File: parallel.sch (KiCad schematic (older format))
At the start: 76 parts, among them CN300 KEYBOARD, CN301 CENTRONICS, CN302 EXTERNAL FLOPPY, CN303 Conn_02x17_Odd_Even, J300 Conn_01x03_Male, J301 DF1:, Q301 2N3904, U102 GARY5719, U108 74LS74A, U203 74LS38, U300 CIA8520, U302 74LS32, U303 74F08, U607 74LS08, U900 74F00

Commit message: Misread the PCB; It's effectively E and not A1
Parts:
- removed C2: 270pF, symbol Device:C
- removed R3: 68, symbol Device:R
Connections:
- wire segments 614 -> 613
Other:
- note removed: "REV 6.2 fixes\n"the via" is A11 line tied to GND\nthrough C and R"
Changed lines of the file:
@@
 Text GLabel 15150 8250 2    50   Input ~ 0
 _BRST
-Entry Wire Line
-	1450 4350 1550 4450
-Wire Wire Line
-	1450 4350 1450 3600
-$Comp
-L Device:C C2
-U 1 1 5D447991
-P 1450 3450
-F 0 "C2" H 1565 3496 50  0000 L CNN
-F 1 "270pF" H 1565 3405 50  0000 L CNN
-F 2 "" H 1488 3300 50  0001 C CNN
-F 3 "~" H 1450 3450 50  0001 C CNN
-	1    1450 3450
-	1    0    0    -1
-$EndComp
-$Comp
-L Device:R R3
-U 1 1 5D4491FD
-P 1450 3150
-F 0 "R3" H 1520 3196 50  0000 L CNN
-F 1 "68" H 1520 3105 50  0000 L CNN
-F 2 "" V 1380 3150 50  0001 C CNN
-F 3 "~" H 1450 3150 50  0001 C CNN
-	1    1450 3150
-	1    0    0    -1
-$EndComp
-$Comp
-L power:GND #PWR0217
-U 1 1 5D44A7A4
-P 1450 3000
-F 0 "#PWR0217" H 1450 2750 50  0001 C CNN
-F 1 "GND" H 1455 2827 50  0000 C CNN
-F 2 "" H 1450 3000 50  0001 C CNN
-F 3 "" H 1450 3000 50  0001 C CNN
-	1    1450 3000
-	-1   0    0    1
-$EndComp
-Text Notes 1000 2700 0    50   ~ 0
-REV 6.2 fixes\n"the via" is A11 line tied to GND\nthrough C and R
 Text Notes 3050 6600 0    50   ~ 0
 REV 6.2 fixes list C909 as removed but I haven't seen\nit removed at all on numerous 6.2 boards.\nso it is kept here
@@
 Wire Bus Line
 	4950 5000 4950 5900
-Text Label 1450 3850 1    50   ~ 0
-A11
 $EndSCHEMATC

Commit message: Add gender to connectors
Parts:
- CN300, CN302: Gender (none) -> Female
- CN301: symbol Connector:DB25_Female -> Connector:DB25_Female_MountingHoles; Gender (none) -> Female
- CN303: Gender (none) -> Male
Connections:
- wire segments 613 -> 614
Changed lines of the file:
@@
 F 2 "" H 13100 2350 50  0001 C CNN
 F 3 " ~" H 13100 2350 50  0001 C CNN
+F 4 "Female" V 13150 2450 50  0001 C CNN "Gender"
 	1    13150 2450
 	0    -1   1    0
@@
 F 2 "" H 15650 5400 50  0001 C CNN
 F 3 "~" H 15650 5400 50  0001 C CNN
+F 4 "Male" H 15650 5400 50  0001 C CNN "Gender"
 	1    15650 5400
 	-1   0    0    -1
 $EndComp
 $Comp
-L Connector:DB25_Female CN301
+L Connector:DB25_Female_MountingHoles CN301
 U 1 1 6B84D7F5
 P 9150 5750
@@
 F 2 "" H 9150 5750 50  0001 C CNN
 F 3 " ~" H 9150 5750 50  0001 C CNN
+F 4 "Female" H 9150 5750 50  0001 C CNN "Gender"
 	1    9150 5750
 	1    0    0    -1
@@
 F 2 "" H 10100 1200 50  0001 C CNN
 F 3 "http://www.mouser.com/ds/2/18/40_c091_abd_e-75918.pdf" H 10100 1200 50  0001 C CNN
+F 4 "Female" H 10100 1200 50  0001 C CNN "Gender"
 	1    10100 1200
 	1    0    0    1
@@
 L power:GND #PWR0182
 U 1 1 6B8C755F
-P 8750 7150
-F 0 "#PWR0182" H 8750 6900 50  0001 C CNN
-F 1 "GND" H 8755 6977 50  0000 C CNN
-F 2 "" H 8750 7150 50  0001 C CNN
-F 3 "" H 8750 7150 50  0001 C CNN
-	1    8750 7150
+P 8750 7200
+F 0 "#PWR0182" H 8750 6950 50  0001 C CNN
+F 1 "GND" H 8755 7027 50  0000 C CNN
+F 2 "" H 8750 7200 50  0001 C CNN
+F 3 "" H 8750 7200 50  0001 C CNN
+	1    8750 7200
 	1    0    0    -1
 $EndComp
@@
 	8850 6850 8750 6850
 Wire Wire Line
-	8750 6850 8750 7100
-Connection ~ 8750 7100
-Wire Wire Line
-	8750 7100 8750 7150
+	8750 6850 8750 7150
+Connection ~ 8750 7150
 Wire Wire Line
 	8850 6650 8750 6650
@@
 Connection ~ 8500 4450
 Wire Wire Line
-	7800 6350 7800 7100
-Wire Wire Line
-	7800 7100 8100 7100
-Wire Wire Line
-	7300 7100 7800 7100
-Connection ~ 7800 7100
+	7800 6350 7800 7150
+Wire Wire Line
+	7800 7150 8100 7150
+Wire Wire Line
+	7300 7150 7800 7150
+Connection ~ 7800 7150
 Wire Wire Line
 	7800 6050 8200 6050
@@
 Connection ~ 7300 6650
 Wire Wire Line
-	7300 6650 7300 7100
+	7300 6650 7300 7150
 Wire Wire Line
 	7550 5900 7550 5600
@@
 $EndComp
 Wire Wire Line
-	8100 7250 8100 7100
-Connection ~ 8100 7100
-Wire Wire Line
-	8100 7100 8750 7100
+	8100 7250 8100 7150
+Connection ~ 8100 7150
+Wire Wire Line
+	8100 7150 8750 7150
 Wire Wire Line
 	8300 3850 8150 3850
@@
 Text Notes 3050 6600 0    50   ~ 0
 REV 6.2 fixes list C909 as removed but I haven't seen\nit removed at all on numerous 6.2 boards.\nso it is kept here
+Wire Wire Line
+	9150 7150 8750 7150
+Wire Wire Line
+	8750 7150 8750 7200
 Wire Bus Line
 	1200 4450 3050 4450

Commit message: whoopsie
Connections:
- net _DKRD: no longer CN303.12 (Pin_12), U900.5
- new net _SEL1: CN303.12 (Pin_12), U900.5
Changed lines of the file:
@@
 Wire Wire Line
 	11100 1150 11100 6000
-Wire Wire Line
-	11100 6000 15300 6000
 Connection ~ 11700 1150
-Text Label 15300 6000 2    50   ~ 0
+Text Label 15250 6000 2    50   ~ 0
 _DKRD
 Wire Wire Line
@@
 Wire Wire Line
 	15950 6750 15950 8950
-Connection ~ 15300 6000
-Wire Wire Line
-	15300 6000 15350 6000
 Wire Wire Line
 	15300 6000 15300 6750
@@
 Wire Bus Line
 	4950 5000 4950 5900
+Wire Wire Line
+	11100 6000 15350 6000
 $EndSCHEMATC

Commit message: kbd ok
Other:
- note removed: "TODO: keyboard connector to be checked..."
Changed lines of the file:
@@
 	1    0    0    1
 $EndComp
-Text Notes 9350 750  0    50   ~ 0
-TODO: keyboard connector to be checked...
 $Comp
 L Device:Ferrite_Bead_Small FB301
@@
 Wire Wire Line
 	8750 7150 8750 7200
+Wire Wire Line
+	11100 6000 15350 6000
 Wire Bus Line
 	1200 4450 3050 4450
@@
 Wire Bus Line
 	4950 5000 4950 5900
-Wire Wire Line
-	11100 6000 15350 6000
 $EndSCHEMATC

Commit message: Review done
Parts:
- R310: value 47 .5W -> 47 0.5W
- R914: value 1 .5W -> 1 0.5W
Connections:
- net GND: now also EMI311.2, EMI312.2, EMI313.2, EMI314.2, EMI315.2, EMI316.2, EMI317.2, EMI322.2, EMI324.2, EMI339.2, EMI340.2, EMI341.2
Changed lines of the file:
@@
 P 8350 850
 F 0 "R914" H 8420 896 50  0000 L CNN
-F 1 "1 .5W" H 8420 805 50  0000 L CNN
+F 1 "1 0.5W" H 8420 805 50  0000 L CNN
 F 2 "" V 8280 850 50  0001 C CNN
 F 3 "~" H 8350 850 50  0001 C CNN
@@
 P 7950 4000
 F 0 "R310" V 7743 4000 50  0000 C CNN
-F 1 "47 .5W" V 7834 4000 50  0000 C CNN
+F 1 "47 0.5W" V 7834 4000 50  0000 C CNN
 F 2 "" V 7880 4000 50  0001 C CNN
 F 3 "~" H 7950 4000 50  0001 C CNN
@@
 L power:+5V #PWR0191
 U 1 1 6BF36D02
-P 15200 3650
-F 0 "#PWR0191" H 15200 3500 50  0001 C CNN
-F 1 "+5V" H 15215 3823 50  0000 C CNN
-F 2 "" H 15200 3650 50  0001 C CNN
-F 3 "" H 15200 3650 50  0001 C CNN
-	1    15200 3650
-	1    0    0    -1
+P 15350 3600
+F 0 "#PWR0191" H 15350 3450 50  0001 C CNN
+F 1 "+5V" V 15350 3800 50  0000 C CNN
+F 2 "" H 15350 3600 50  0001 C CNN
+F 3 "" H 15350 3600 50  0001 C CNN
+	1    15350 3600
+	0    1    1    0
 $EndComp
 $Comp
@@
 Wire Wire Line
 	11100 6000 15350 6000
+$Comp
+L power:GND #PWR0271
+U 1 1 5D173C28
+P 15350 3400
+F 0 "#PWR0271" H 15350 3150 50  0001 C CNN
+F 1 "GND" V 15355 3272 50  0000 R CNN
+F 2 "" H 15350 3400 50  0001 C CNN
+F 3 "" H 15350 3400 50  0001 C CNN
+	1    15350 3400
+	0    -1   -1   0
+$EndComp
+Wire Wire Line
+	15350 3400 15200 3400
+Connection ~ 15200 3400
+Wire Wire Line
+	15350 3600 15200 3600
+Wire Wire Line
+	15200 3600 15200 3650
 Wire Bus Line
 	1200 4450 3050 4450

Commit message: Associate footprints with components
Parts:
- CN303: footprint (none) -> Connector_PinSocket_2.54mm:PinSocket_2x17_P2.54mm_Vertical
- EMI300, EMI301, EMI302, EMI303, EMI304, EMI305, EMI306, EMI307, EMI308, EMI309, EMI310, EMI311, EMI312, EMI313, EMI314, EMI315, EMI316, EMI317, EMI318, EMI319, EMI320, EMI321, EMI322, EMI323, EMI324, EMI335, EMI336, EMI337, EMI338, EMI339, EMI340, EMI341, J300: footprint (none) -> Connector_PinSocket_2.54mm:PinSocket_1x03_P2.54mm_Vertical
- F3, F4: footprint (none) -> Fuse:Fuse_Littelfuse-LVR100
- FB301, FB302, FB303: footprint (none) -> Inductor_THT:L_Axial_L7.0mm_D3.3mm_P10.16mm_Horizontal_Fastron_MICC
- J301: footprint (none) -> Connector_PinSocket_2.54mm:PinSocket_2x01_P2.54mm_Vertical
- R201, R300, R301, R309, R602: footprint (none) -> Resistor_THT:R_Axial_DIN0207_L6.3mm_D2.5mm_P10.16mm_Horizontal
- R310, R914: footprint (none) -> Resistor_THT:R_Axial_DIN0411_L9.9mm_D3.6mm_P15.24mm_Horizontal
- U102: footprint (none) -> Package_DIP:DIP-48_W15.24mm_Socket
- U108, U203, U302, U303, U607, U900: footprint (none) -> Package_DIP:DIP-14_W7.62mm_Socket
- U300: footprint (none) -> Package_DIP:DIP-40_W15.24mm_Socket

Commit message: Associate more components
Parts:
- C912: value 470uF -> 470uF 25v; footprint (none) -> Capacitor_THT:CP_Radial_D10.0mm_P5.00mm
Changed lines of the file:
@@
 P 10350 1800
 F 0 "C912" H 10468 1846 50  0000 L CNN
-F 1 "470uF" H 10468 1755 50  0000 L CNN
-F 2 "" H 10388 1650 50  0001 C CNN
+F 1 "470uF 25v" H 10468 1755 50  0000 L CNN
+F 2 "Capacitor_THT:CP_Radial_D10.0mm_P5.00mm" H 10388 1650 50  0001 C CNN
 F 3 "~" H 10350 1800 50  0001 C CNN
 	1    10350 1800

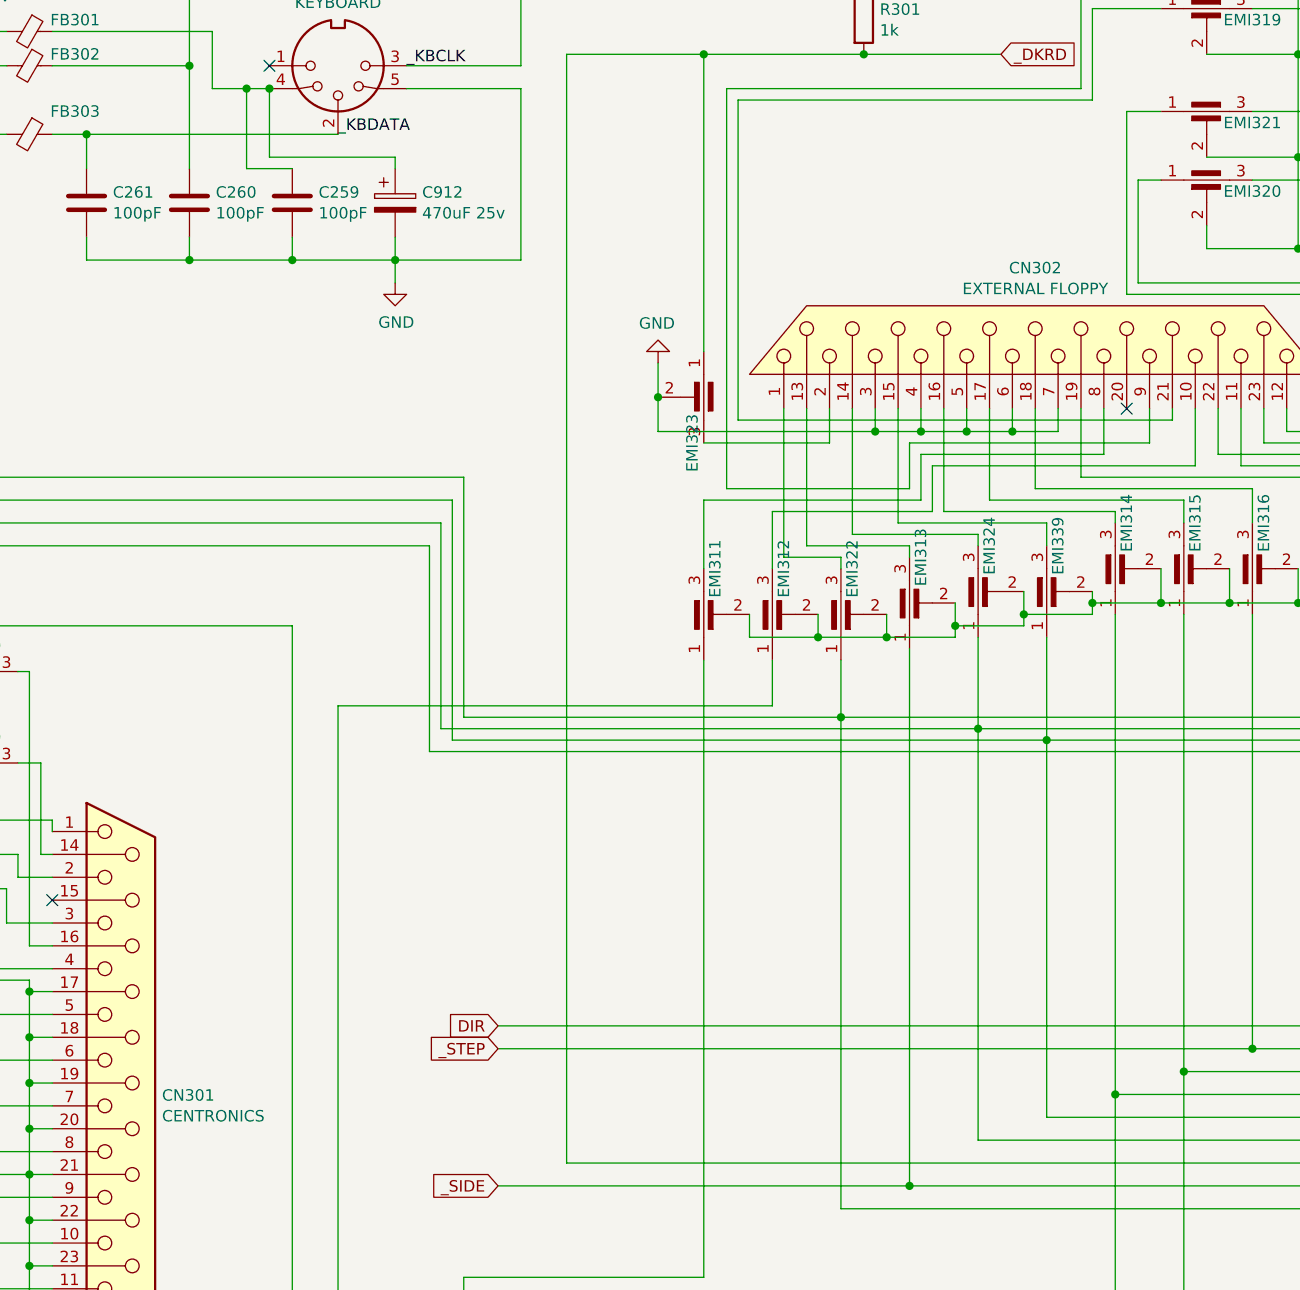
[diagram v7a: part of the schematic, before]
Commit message: Change namings
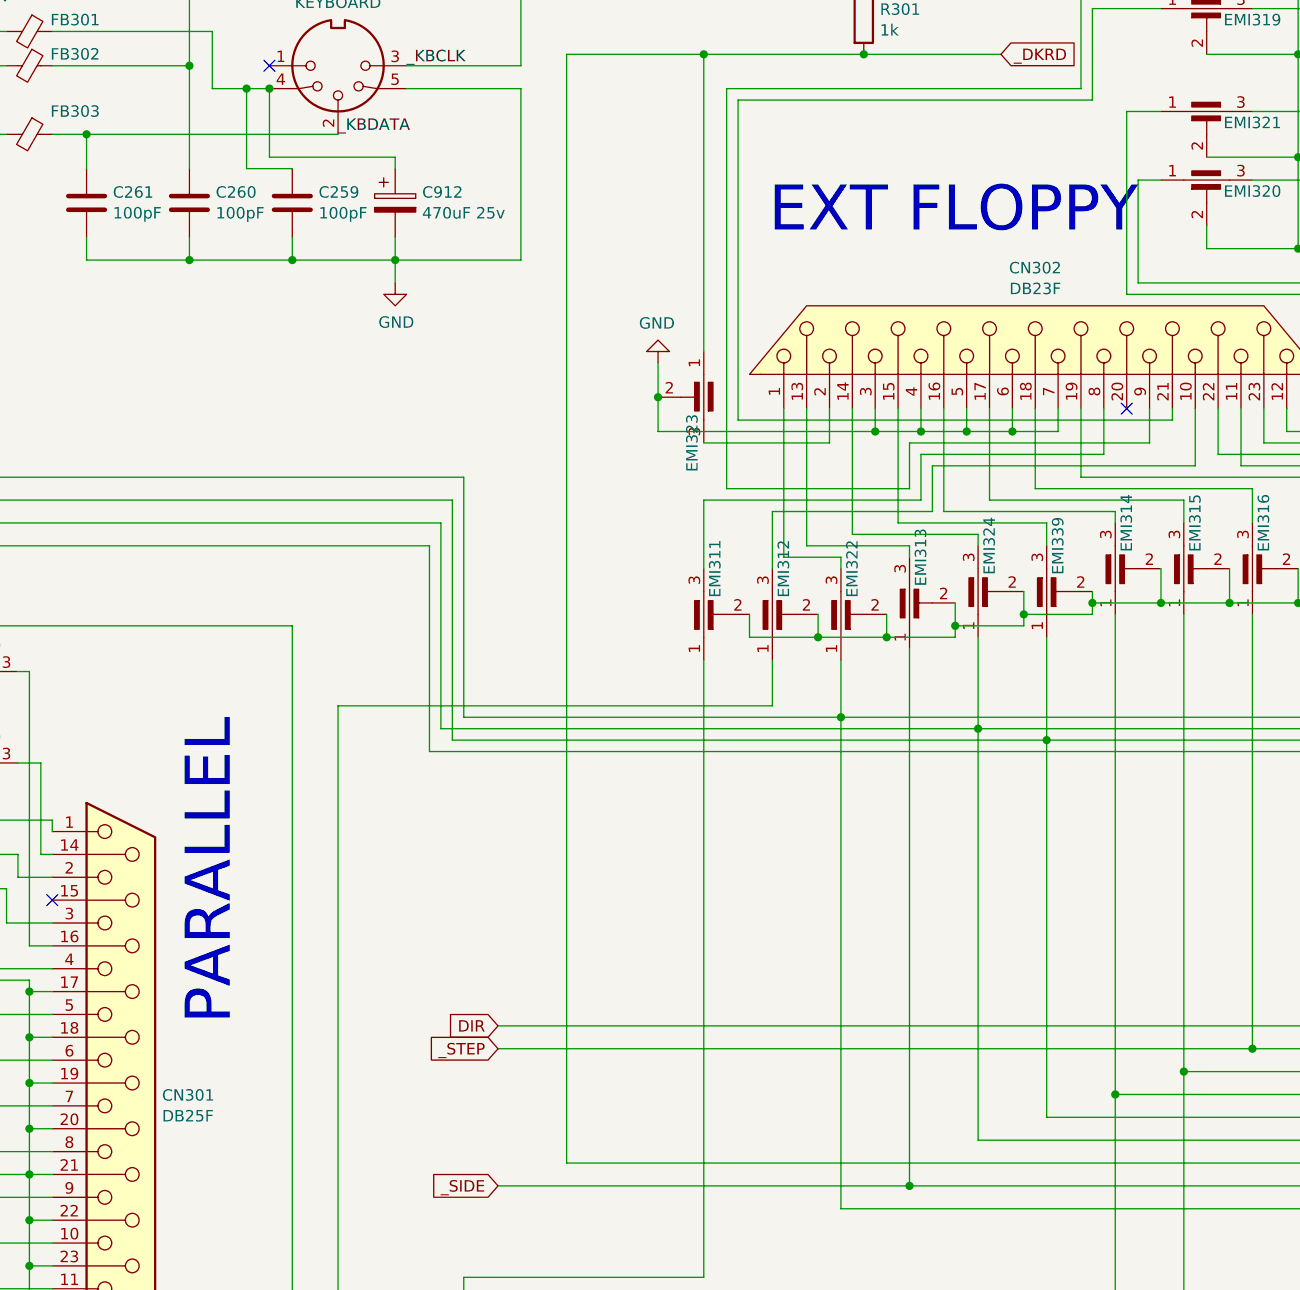
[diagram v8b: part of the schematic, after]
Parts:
- CN301: value CENTRONICS -> DB25F; footprint (none) -> Connector_Dsub:DSUB-25_Female_Horizontal_P2.77x2.84mm_EdgePinOffset7.70mm_Housed_MountingHolesOffset9.12mm
- CN302: value EXTERNAL FLOPPY -> DB23F
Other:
- note added: "EXT FLOPPY"
- note added: "PARALLEL"
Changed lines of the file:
@@
 P 13150 2450
 F 0 "CN302" V 12785 2450 50  0000 C CNN
-F 1 "EXTERNAL FLOPPY" V 12876 2450 50  0000 C CNN
+F 1 "DB23F" V 12876 2450 50  0000 C CNN
 F 2 "" H 13100 2350 50  0001 C CNN
 F 3 " ~" H 13100 2350 50  0001 C CNN
@@
 P 9150 5750
 F 0 "CN301" H 9330 5796 50  0000 L CNN
-F 1 "CENTRONICS" H 9330 5705 50  0000 L CNN
-F 2 "" H 9150 5750 50  0001 C CNN
+F 1 "DB25F" H 9330 5705 50  0000 L CNN
+F 2 "Connector_Dsub:DSUB-25_Female_Horizontal_P2.77x2.84mm_EdgePinOffset7.70mm_Housed_MountingHolesOffset9.12mm" H 9150 5750 50  0001 C CNN
 F 3 " ~" H 9150 5750 50  0001 C CNN
 F 4 "Female" H 9150 5750 50  0001 C CNN "Gender"
@@
 Wire Bus Line
 	4950 5000 4950 5900
+Text Notes 9650 5400 1    197  ~ 0
+PARALLEL
+Text Notes 13600 1950 2    197  ~ 0
+EXT FLOPPY
 $EndSCHEMATC
